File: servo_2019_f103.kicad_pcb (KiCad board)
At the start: 2 copper layers, 24 parts, among them J1 alim_logique_5V, Q1 BSS138, Q2 BSS138, Q3 2N2222, Q4 2N2222, Q5 2N2222, U2 TC1262-33, U3 w5500, U4 servo_connector

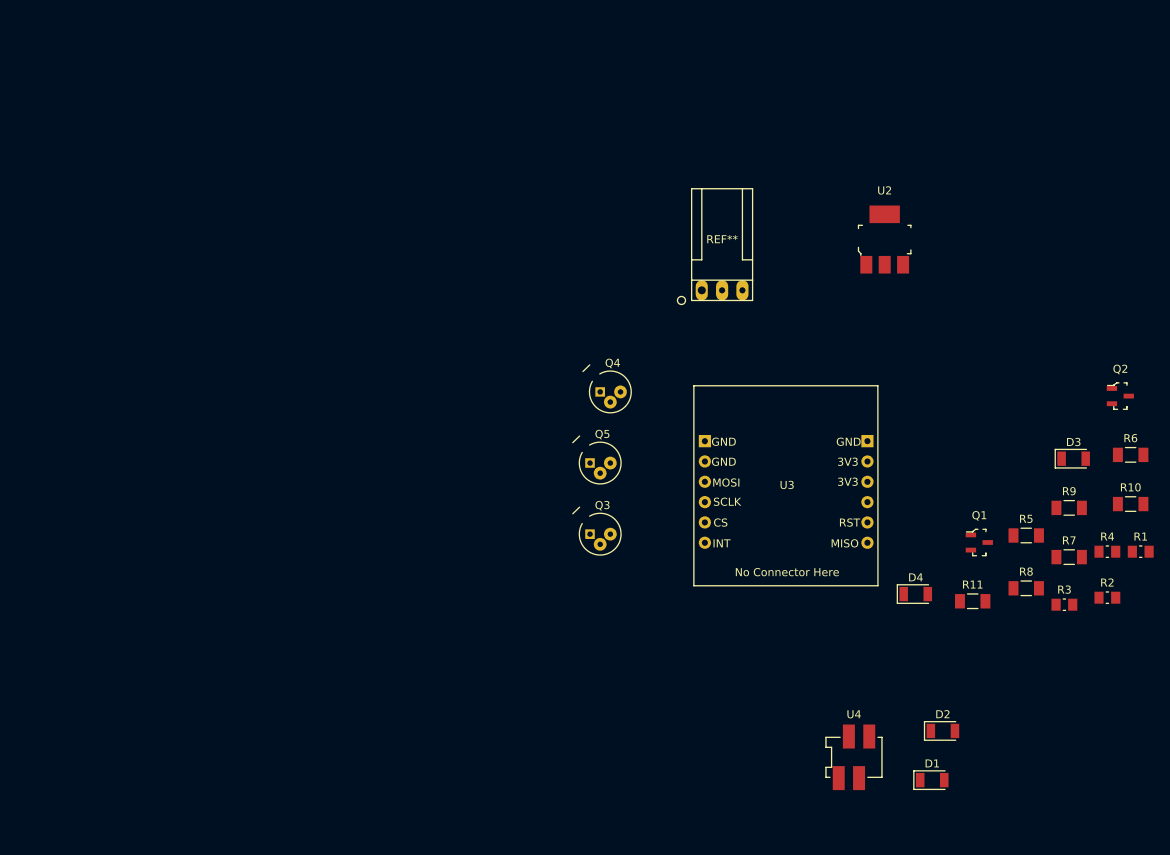
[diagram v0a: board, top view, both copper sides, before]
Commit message: Import generic card template
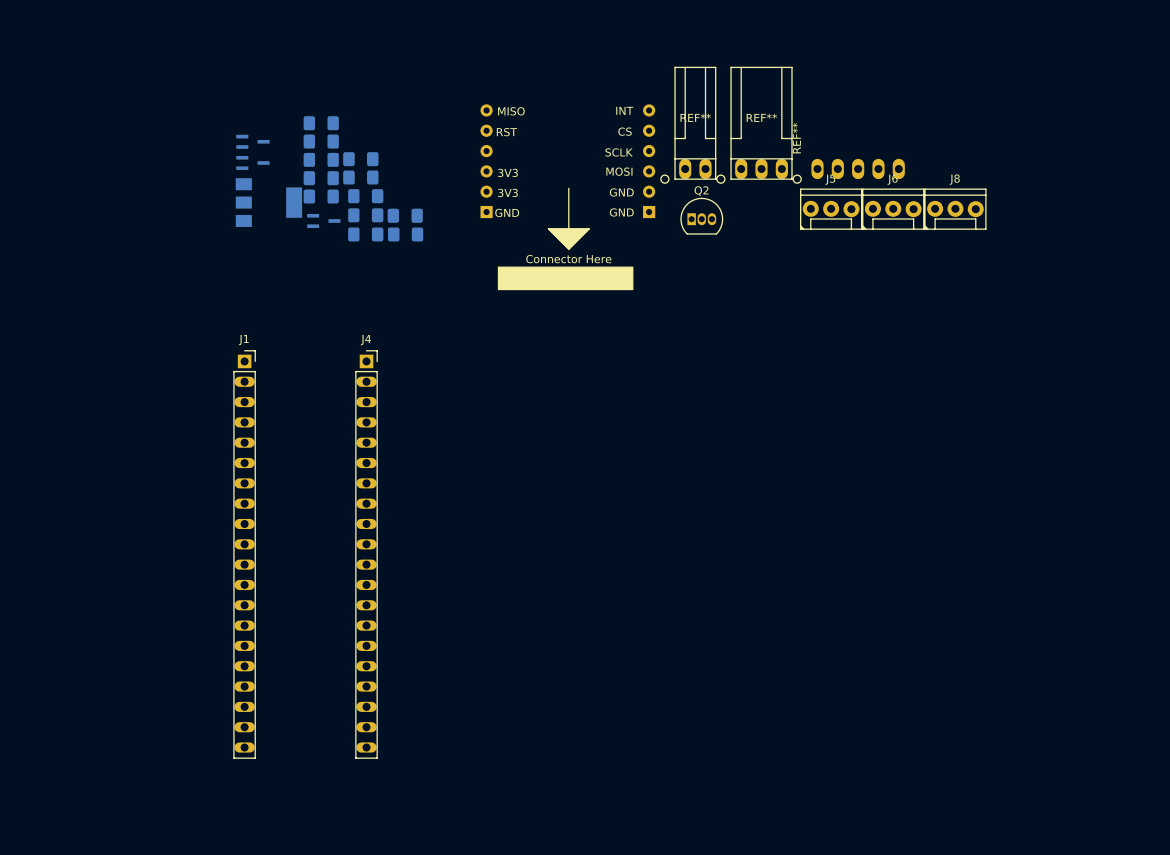
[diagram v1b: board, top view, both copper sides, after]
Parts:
- removed Q5: 2N2222, digikey-footprints:TO-18-3
- removed R10, R8: 1kR, Resistor_SMD:R_1206_3216Metric_Pad1.24x1.80mm_HandSolder
- removed R11, R7, R9: 100R, Resistor_SMD:R_1206_3216Metric_Pad1.24x1.80mm_HandSolder
- removed U3: w5500, @Robot:w5500
- removed U4: servo_connector, @Robot:ConnectorMicromatch-4
- added C1: 1u, Capacitor_SMD:C_1206_3216Metric_Pad1.42x1.75mm_HandSolder, B.Cu at (126.4, 58.1)
- added C2: 1u, Capacitor_SMD:C_1206_3216Metric_Pad1.42x1.75mm_HandSolder, B.Cu at (126.4, 55.8)
- added J2: Alim puissance, @Robot:HE14-2_horizontal, F.Cu at (173.2, 50.9)
- added J3: Alim logique, @Robot:HE14-3_horizontal, F.Cu at (181.5, 50.9)
- added J4: Conn_01x20_Female, @Robot:PinSocket_1x20_P2.54mm_Vertical_Long_Pads, F.Cu at (132.1, 78.7)
- added J5: PWM input, @Robot:HE14-3-straight, F.Cu at (190.2, 58.9)
- added J6: PWM output, @Robot:HE14-3-straight, F.Cu at (197.9, 58.9)
- added J7: QEI, @Robot:HE14-5_horizontal, F.Cu at (191.0, 50.9)
- added J8: Liaison serie, @Robot:HE14-3-straight, F.Cu at (205.7, 58.9)
- added U1: TC1262-33, Package_TO_SOT_SMD:SOT-223-3_TabPin2, B.Cu at (119.9, 58.9)
- D1: value LED_RED -> LED_hardfault_jaune; footprint LED_SMD:LED_1206_3216Metric_Pad1.07x1.80mm_HandSolder -> LED_SMD:LED_1206_3216Metric_Pad1.42x1.75mm_HandSolder; moved to B.Cu
- D2: value LED_YELLOW -> LED_communication_vert; footprint LED_SMD:LED_1206_3216Metric_Pad1.07x1.80mm_HandSolder -> LED_SMD:LED_1206_3216Metric_Pad1.42x1.75mm_HandSolder; moved to B.Cu
- D3: value LED_GREEN -> led_feedback_vert; footprint LED_SMD:LED_1206_3216Metric_Pad1.07x1.80mm_HandSolder -> LED_SMD:LED_1206_3216Metric_Pad1.42x1.75mm_HandSolder; moved to B.Cu
- D4: value LED_GREEN -> LED_alimentation_rouge; footprint LED_SMD:LED_1206_3216Metric_Pad1.07x1.80mm_HandSolder -> LED_SMD:LED_1206_3216Metric_Pad1.42x1.75mm_HandSolder; moved to B.Cu
- J1: value alim_logique_5V -> Conn_01x20_Female; footprint @Robot:HE14-3_horizontal -> @Robot:PinSocket_1x20_P2.54mm_Vertical_Long_Pads
- Q1: value BSS138 -> PMF370XN; footprint digikey-footprints:SOT-23-3 -> Package_TO_SOT_SMD:SOT-323_SC-70_Handsoldering; moved to B.Cu
- Q2: value BSS138 -> 2N7000; footprint digikey-footprints:SOT-23-3 -> Package_TO_SOT_THT:TO-92_Inline
- Q3, Q4: value 2N2222 -> PMF370XN; footprint digikey-footprints:TO-18-3 -> Package_TO_SOT_SMD:SOT-323_SC-70_Handsoldering; moved to B.Cu
- R1, R4: value 10k -> 150; footprint Resistor_SMD:R_0805_2012Metric_Pad1.15x1.50mm_HandSolder -> Resistor_SMD:R_1206_3216Metric_Pad1.42x1.75mm_HandSolder; moved to B.Cu
- R2, R3: value 10k -> R; footprint Resistor_SMD:R_0805_2012Metric_Pad1.15x1.50mm_HandSolder -> Resistor_SMD:R_1206_3216Metric_Pad1.42x1.75mm_HandSolder; moved to B.Cu
- R5: value 100R -> 150; footprint Resistor_SMD:R_1206_3216Metric_Pad1.24x1.80mm_HandSolder -> Resistor_SMD:R_1206_3216Metric_Pad1.42x1.75mm_HandSolder; moved to B.Cu
- R6: value 1kR -> 150; footprint Resistor_SMD:R_1206_3216Metric_Pad1.24x1.80mm_HandSolder -> Resistor_SMD:R_1206_3216Metric_Pad1.42x1.75mm_HandSolder; moved to B.Cu
- U2: value TC1262-33 -> w5500; footprint digikey-footprints:SOT-223 -> @Robot:w5500
- moved R1 113.5 mm to (126.4, 53.5)
- moved R4 110.8 mm to (126.4, 51.3)
- moved R2 107.1 mm to (131.4, 55.7)
- moved R3 104.1 mm to (131.4, 53.5)
- moved R5 102.1 mm to (126.4, 49.0)
- moved D1 98.3 mm to (132.0, 62.9)
- moved R6 95.5 mm to (136.9, 60.5)
- moved D3 93.6 mm to (132.0, 60.5)
- moved D2 91.4 mm to (137.0, 62.9)
- moved Q1 91.3 mm to (126.7, 61.2)
- moved D4 84.9 mm to (132.0, 58.1)
- moved Q3 62.7 mm to (117.9, 53.9)
- moved J1 61.0 mm to (116.8, 78.7)
- moved Q2 58.0 mm to (172.7, 61.0)
- moved Q4 53.5 mm to (117.9, 51.3)
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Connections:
- J1 pad 1: +5V -> Net-(J1-Pad1)
- J1 pad 2: GND -> Net-(J1-Pad2)
- Q1 pad 1: /µCTX -> /led_hardfault
- Q1 pad 2: +3V3 -> GND
- Q1 pad 3: +5V -> Net-(D1-Pad1)
- Q2 pad 1: /µCRX -> /3.3V_logic
- Q2 pad 3: +5V -> /5V_logic
- Q3 pad 1: Net-(D1-Pad1) -> /TX
- Q3 pad 2: Net-(Q3-Pad2) -> GND
- Q3 pad 3: GND -> Net-(D2-Pad1)
- Q4 pad 1: Net-(D2-Pad1) -> /led_feedback
- Q4 pad 2: Net-(Q4-Pad2) -> GND
- Q4 pad 3: GND -> Net-(D3-Pad1)
- R1 pad 2: /ServoRX -> Net-(D1-Pad2)
- R2 pad 2: /µCTX -> /3.3V_logic
- R3 pad 1: +3V3 -> +5V
- R3 pad 2: /µCRX -> /5V_logic
- R4 pad 2: /ServoTX -> Net-(D2-Pad2)
- R5 pad 1: Net-(D1-Pad2) -> +5V
- R5 pad 2: +3V3 -> Net-(D3-Pad2)
- R6 pad 1: Net-(Q3-Pad2) -> +5V
- R6 pad 2: /HardFault -> Net-(D4-Pad2)
- U2 pad 1: +5V -> Net-(U2-Pad1)
- U2 pad 2: GND -> Net-(U2-Pad2)
- U2 pad 3: +3V3 -> Net-(U2-Pad3)
- U2 pad 4: (no net) -> Net-(U2-Pad4)
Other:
- rule pad_to_mask_clearance: 0.2 -> 0.051

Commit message: update first try at rooting
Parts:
- removed D2: LED_communication_vert, LED_SMD:LED_1206_3216Metric_Pad1.42x1.75mm_HandSolder
- removed J2: Alim puissance, @Robot:HE14-2_horizontal
- removed J5: PWM input, @Robot:HE14-3-straight
- removed J6: PWM output, @Robot:HE14-3-straight
- removed J7: QEI, @Robot:HE14-5_horizontal
- removed J8: Liaison serie, @Robot:HE14-3-straight
- removed Q3: PMF370XN, Package_TO_SOT_SMD:SOT-323_SC-70_Handsoldering
- removed R4: 150, Resistor_SMD:R_1206_3216Metric_Pad1.42x1.75mm_HandSolder
- added Q5: 2N7000, Package_TO_SOT_THT:TO-92_Inline, F.Cu at (136.8, 85.5)
- added R7: 10kR, Resistor_SMD:R_1206_3216Metric_Pad1.39x1.80mm_HandSolder, B.Cu at (136.0, 79.7)
- added R8: 10kR, Resistor_SMD:R_1206_3216Metric_Pad1.39x1.80mm_HandSolder, B.Cu at (141.2, 80.0)
- added U3: servo_connector, Connector_PinHeader_2.54mm:PinHeader_2x02_P2.54mm_Vertical, F.Cu at (144.2, 88.8)
- R2, R3: value R -> 10kR
- moved Q4 80.8 mm to (144.8, 127.5), turned to 180 degrees
- moved R5 72.1 mm to (138.8, 120.0)
- moved J3 71.4 mm to (149.1, 114.5), turned to 270 degrees
- moved R1 70.1 mm to (111.3, 122.0), turned to 180 degrees
- moved D3 67.4 mm to (138.7, 127.5), turned to 180 degrees
- moved D1 57.0 mm to (111.2, 116.0)
- moved C1 55.4 mm to (124.3, 113.5)
- moved R6 51.0 mm to (139.0, 111.5), turned to 180 degrees
- moved Q1 50.1 mm to (111.0, 108.8), turned to 180 degrees
- moved D4 49.4 mm to (139.0, 107.0), turned to 180 degrees
- moved R3 47.9 mm to (143.8, 99.8), turned to 90 degrees
- moved Q2 47.3 mm to (136.8, 91.8)
- moved R2 44.7 mm to (135.2, 100.3), turned to 90 degrees
- moved U1 43.8 mm to (125.8, 102.2)
- moved C2 36.0 mm to (123.8, 91.8)
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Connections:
- net /5V_logic renamed /5V_logic_tx
- J1 pad 11: Net-(J1-Pad11) -> /sck
- J1 pad 12: Net-(J1-Pad12) -> /miso
- J1 pad 13: Net-(J1-Pad13) -> /mosi
- J1 pad 15: Net-(J1-Pad15) -> /led_hardfault
- J1 pad 2: Net-(J1-Pad2) -> /cs
- J1 pad 20: +3V3 -> Net-(J1-Pad20)
- J4 pad 3: +3V3 -> Net-(J4-Pad3)
- J4 pad 5: Net-(J4-Pad5) -> /3.3V_logic_rx
- J4 pad 6: Net-(J4-Pad6) -> /3.3V_logic_tx
- Q2 pad 1: /3.3V_logic -> /3.3V_logic_tx
- R2 pad 2: /3.3V_logic -> /3.3V_logic_tx
- U2 pad 2: Net-(U2-Pad2) -> /cs
- U2 pad 3: Net-(U2-Pad3) -> /sck
- U2 pad 4: Net-(U2-Pad4) -> /mosi
- U2 pad 7: Net-(U2-Pad7) -> /miso
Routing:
- net +5V: track 0.00 -> 103.0 mm
- net +3V3: track 0.00 -> 61.0 mm
- net /mosi: track 0.00 -> 57.9 mm
- net /miso: track 0.00 -> 50.9 mm
- net /sck: track 0.00 -> 49.1 mm
- net /cs: track 0.00 -> 22.4 mm
- net /3.3V_logic_tx: track 0.00 -> 13.0 mm
- net /3.3V_logic_rx: track 0.00 -> 11.3 mm
- net /led_hardfault: track 0.00 -> 9.33 mm
- net Net-(D3-Pad2): track 0.00 -> 8.99 mm
- net /5V_logic_tx: track 0.00 -> 8.37 mm
- net Net-(D1-Pad1): track 0.00 -> 7.28 mm
- net Net-(D1-Pad2): track 0.00 -> 7.22 mm
- net /5V_logic_rx: track 0.00 -> 4.80 mm
- net Net-(D4-Pad2): track 0.00 -> 4.51 mm
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- added copper zone on B.Cu, net GND
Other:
- net class Default: clearance 0.2 -> 0.381; trace_width 0.25 -> 0.762
- rule trace_clearance: 0.2 -> 0.381

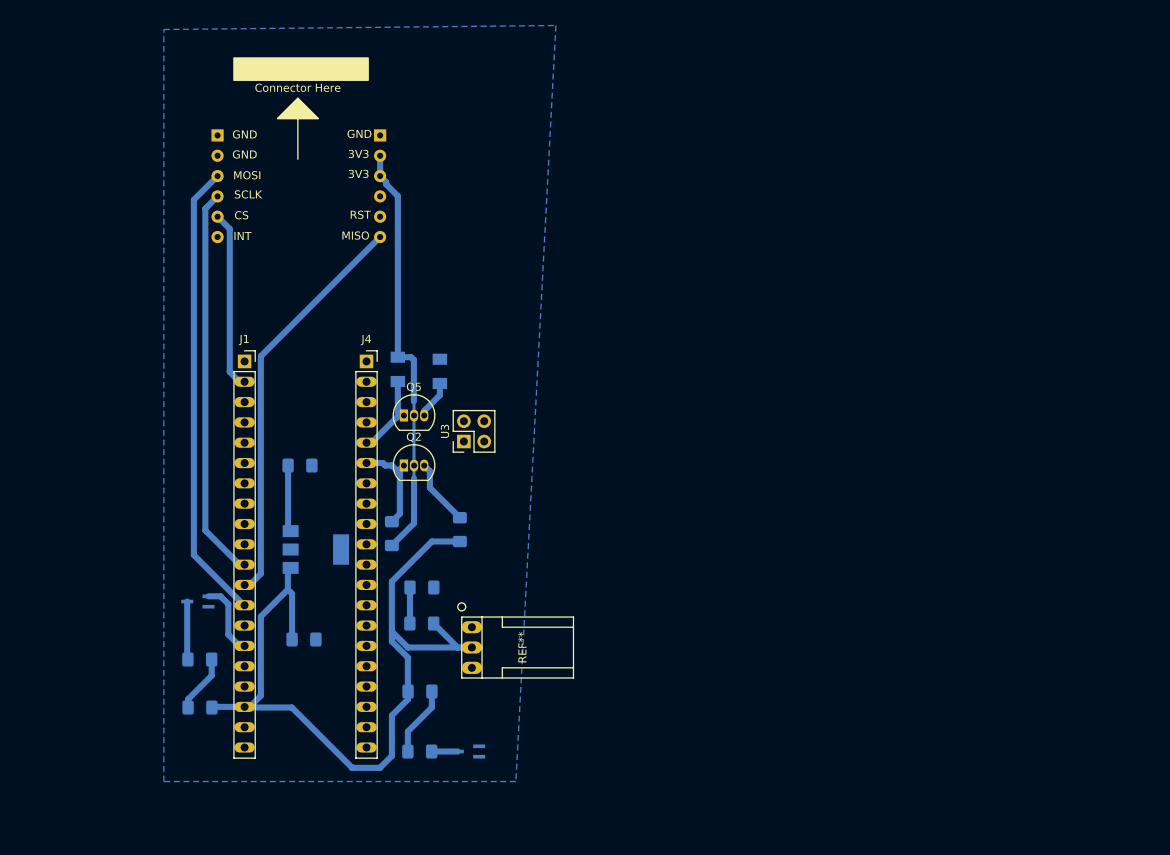
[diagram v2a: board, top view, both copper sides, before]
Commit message: changed the led packages and added missing routes
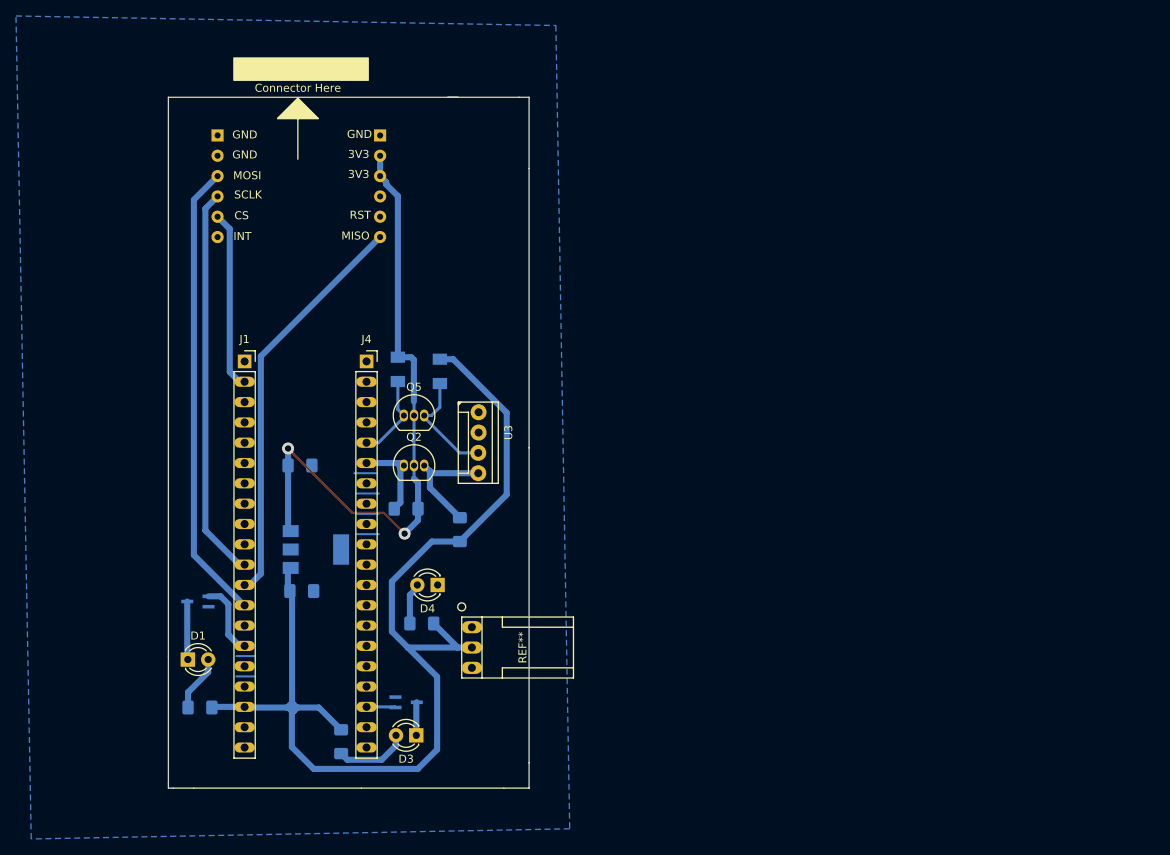
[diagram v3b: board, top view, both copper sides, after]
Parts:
- D1, D3, D4: footprint LED_SMD:LED_1206_3216Metric_Pad1.42x1.75mm_HandSolder -> LED_THT:LED_D3.0mm; moved to F.Cu
- U3: footprint Connector_PinHeader_2.54mm:PinHeader_2x02_P2.54mm_Vertical -> @Robot:HE14-4-straight
- moved R5 11.7 mm to (128.9, 126.3), turned to 270 degrees
- moved Q4 9.93 mm to (137.0, 121.3), turned to 0 degrees
- moved C1 6.06 mm to (124.0, 107.4)
- moved R2 3.58 mm to (137.0, 97.2), turned to 180 degrees
- moved U3 2.82 mm to (146.8, 87.6), turned to 270 degrees
- moved D3 2.07 mm to (138.3, 125.5)
- moved D4 2.00 mm to (141.0, 106.7)
- moved D1 1.49 mm to (109.8, 116.0)
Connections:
- J4 pad 18: Net-(J4-Pad18) -> /led_feedback
- U3 pad 1: /5V_logic_tx -> Net-(U3-Pad1)
- U3 pad 2: /5V_logic_rx -> Net-(U3-Pad2)
- U3 pad 3: Net-(U3-Pad3) -> /5V_logic_rx
- U3 pad 4: Net-(U3-Pad4) -> /5V_logic_tx
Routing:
- net +5V: track 103.0 -> 141.0 mm
- net +3V3: track 61.0 -> 80.3 mm, vias 0 -> 2
- net GND: track 0.00 -> 15.7 mm
- net /5V_logic_rx: track 4.80 -> 14.2 mm
- net /5V_logic_tx: track 8.37 -> 14.9 mm
- net /led_feedback: track 0.00 -> 3.66 mm
- net Net-(D3-Pad1): track 3.28 -> 4.15 mm
- net /3.3V_logic_tx: track 13.0 -> 12.2 mm
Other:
- board outline added: 45.1 x 86.4 mm
- net class Default: via_dia 0.8 -> 1.5; via_drill 0.4 -> 0.8

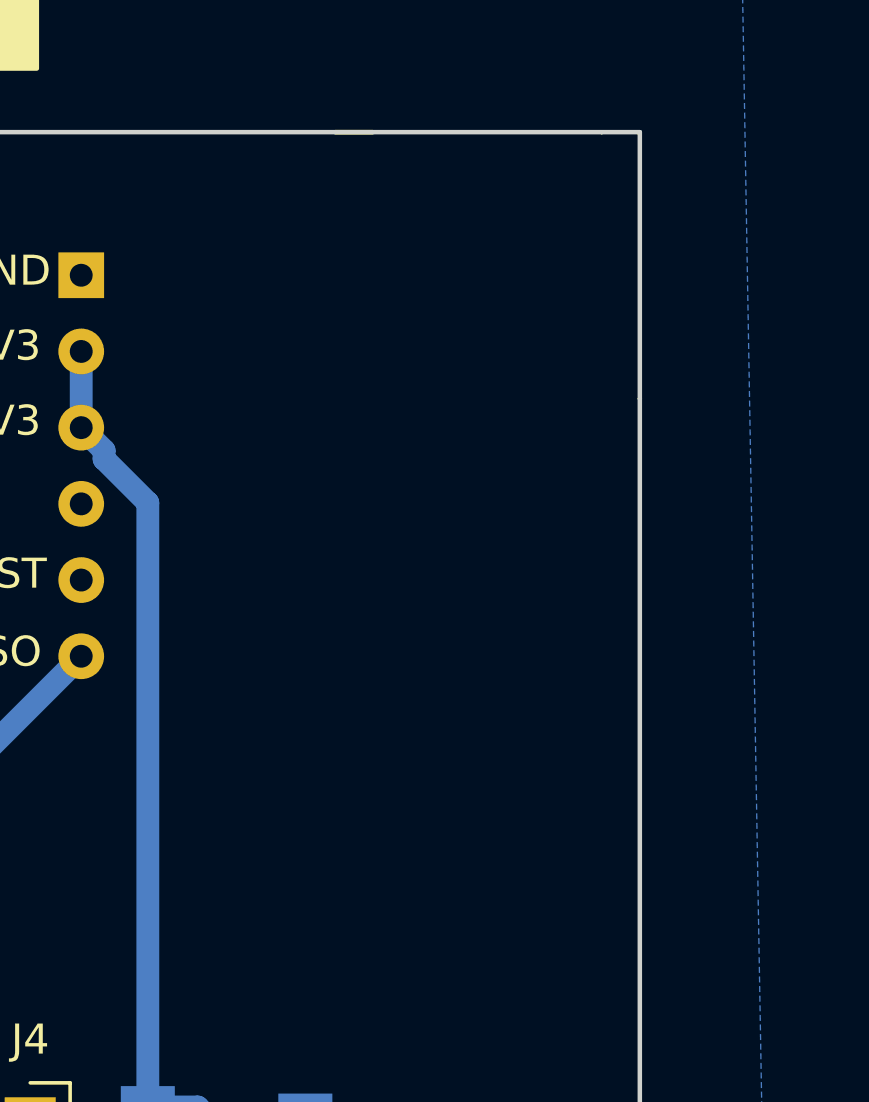
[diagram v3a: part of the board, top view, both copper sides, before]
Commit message: added text to print the card without side mistakes
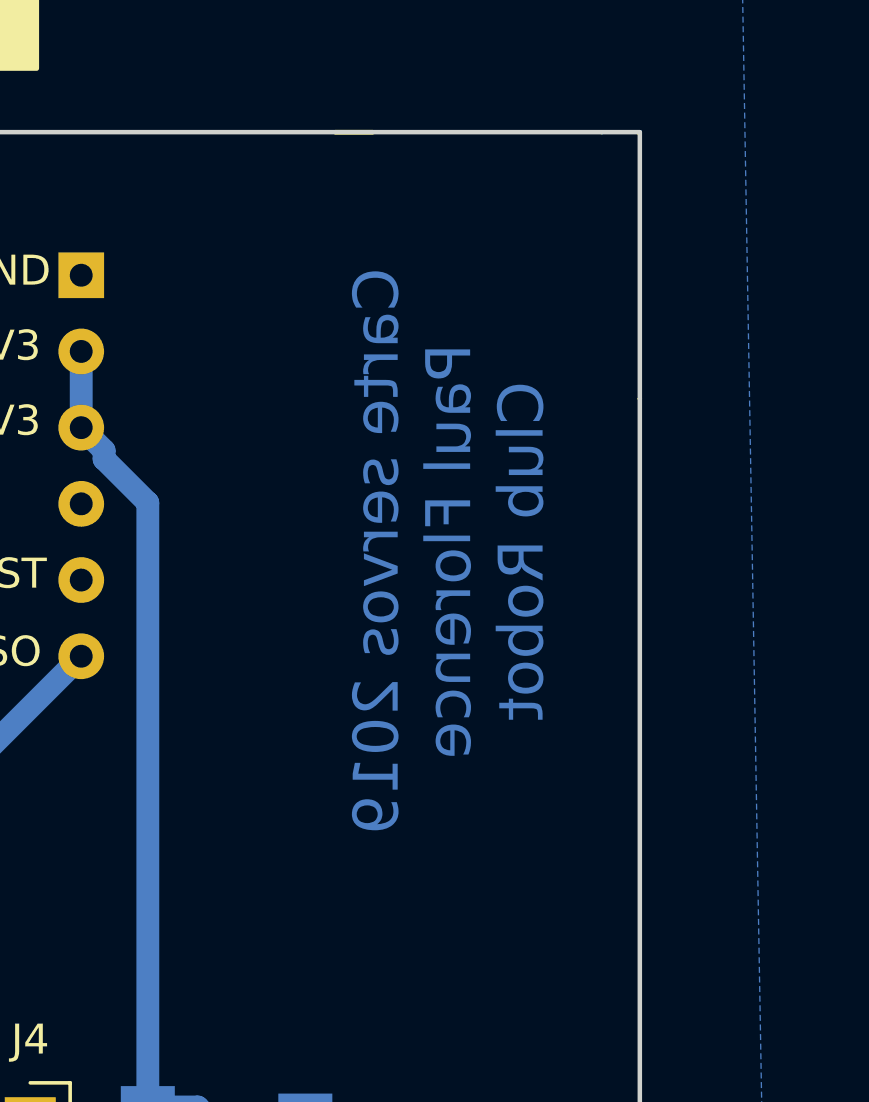
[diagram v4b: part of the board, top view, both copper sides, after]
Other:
- board text added: "Carte servos 2019 Paul Florence Club Robot"
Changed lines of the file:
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@@
   (general
     (thickness 1.6)
-    (drawings 15)
+    (drawings 16)
     (tracks 147)
     (zones 0)
@@
     )
   )
+  (gr_text "Carte servos 2019\nPaul Florence\nClub Robot" (at 146.05 59.69 90) (layer B.Cu)
+    (effects (font (size 1.5 1.5) (thickness 0.3)) (justify mirror))
+  )
   (gr_line (start 152.4 45.72) (end 151.13 45.72) (layer Edge.Cuts) (width 0.15))

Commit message: saved the actual modifications on the schematic
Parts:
- moved C2 4.14 mm to (123.8, 95.9)
- moved R2 1.18 mm to (138.2, 97.2)
- moved C1 1.14 mm to (124.0, 108.6)
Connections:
- J1 pad 16: Net-(J1-Pad16) -> GND
- J4 pad 11: Net-(J4-Pad11) -> GND
- J4 pad 12: Net-(J4-Pad12) -> GND
- J4 pad 8: Net-(J4-Pad8) -> +3V3
- J4 pad 9: Net-(J4-Pad9) -> +3V3
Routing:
- net GND: track 15.7 -> 0.00 mm
- net +3V3: track 80.3 -> 84.2 mm, vias 2 -> 0
- net +5V: track 141.0 -> 142.0 mm
- net /3.3V_logic_tx: track 12.2 -> 11.2 mm
